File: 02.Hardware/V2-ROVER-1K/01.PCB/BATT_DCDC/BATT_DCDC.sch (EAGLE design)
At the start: 44 parts, among them K1 FLEX8, K2 FLEX6, Q1 NVTFS9D6P04M8LTAG, Q2 2N7002PW, Q5 2N7002PW, U1 MCP6071T-E/OT, U3 TPS55330RTET, U7 MCP6071T-E/OT

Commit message: Revision Silk y BOM
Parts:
- R10: value 330 -> 330R
- R3, R7: value 2.4k -> 2k4
- R38, R39: value 78.7k -> 78k7
- R43: value 78.7k -> 30k
- R5: value 33 -> 33R
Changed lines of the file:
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@@
 <part name="L1" library="Inductance_2.2uH" deviceset="74437349100" device="" value="2.2uH - 74437346022"/>
 <part name="D2" library="B520C-13-F" deviceset="B520C-13-F" device=""/>
-<part name="R38" library="SparkFun-Resistors" deviceset="RESISTOR" device="0402" value="78.7k"/>
+<part name="R38" library="SparkFun-Resistors" deviceset="RESISTOR" device="0402" value="78k7"/>
 <part name="GND17" library="SparkFun" deviceset="GND" device=""/>
 <part name="GND24" library="SparkFun" deviceset="GND" device=""/>
@@
 <part name="C19" library="Wurth_Elektronik_Passive_Capacitors_rev19a" library_urn="urn:adsk.eagle:library:491551" deviceset="WCAP-CSGP_1210" device="" package3d_urn="urn:adsk.eagle:package:491820/3" technology="_885012109003" value="47uF 25V"/>
 <part name="GND28" library="SparkFun" deviceset="GND" device=""/>
-<part name="R39" library="SparkFun-Resistors" library_urn="urn:adsk.eagle:library:532" deviceset="RESISTOR" device="0402" package3d_urn="urn:adsk.eagle:package:39657/1" value="78.7k"/>
+<part name="R39" library="SparkFun-Resistors" library_urn="urn:adsk.eagle:library:532" deviceset="RESISTOR" device="0402" package3d_urn="urn:adsk.eagle:package:39657/1" value="78k7"/>
 <part name="C21" library="SparkFun-Capacitors" deviceset="2.2NF/2200PF" device="-0603-50V-10%" value="2.2nF"/>
 <part name="R41" library="SparkFun-Resistors" library_urn="urn:adsk.eagle:library:532" deviceset="RESISTOR" device="0402" package3d_urn="urn:adsk.eagle:package:39657/1" value="56k2"/>
 <part name="C22" library="SparkFun-Capacitors" deviceset="270PF" device="-0603-50V-5%" value="270PF"/>
 <part name="GND30" library="SparkFun" deviceset="GND" device=""/>
-<part name="R43" library="SparkFun-Resistors" deviceset="RESISTOR" device="0402" value="78.7k"/>
+<part name="R43" library="SparkFun-Resistors" deviceset="RESISTOR" device="0402" value="30k"/>
 <part name="C12" library="Wurth_Elektronik_Passive_Capacitors_rev19a" library_urn="urn:adsk.eagle:library:491551" deviceset="WCAP-CSGP_1210" device="" package3d_urn="urn:adsk.eagle:package:491820/3" technology="_885012109003" value="47uF 16V"/>
 <part name="Q2" library="SparkFun-DiscreteSemi" deviceset="MOSFET-NCHANNEL" device="2N7002PW" value="2N7002PW"/>
@@
 <part name="GND9" library="SparkFun" deviceset="GND" device=""/>
 <part name="R4" library="SparkFun-Resistors" library_urn="urn:adsk.eagle:library:532" deviceset="RESISTOR" device="0402" package3d_urn="urn:adsk.eagle:package:39657/1" value="100k"/>
-<part name="R5" library="SparkFun-Resistors" library_urn="urn:adsk.eagle:library:532" deviceset="RESISTOR" device="0402" package3d_urn="urn:adsk.eagle:package:39657/1" value="33"/>
+<part name="R5" library="SparkFun-Resistors" library_urn="urn:adsk.eagle:library:532" deviceset="RESISTOR" device="0402" package3d_urn="urn:adsk.eagle:package:39657/1" value="33R"/>
 <part name="C24" library="SparkFun-Capacitors" deviceset="0.1UF" device="-0603-25V-(+80/-20%)" value="0.1uF"/>
 <part name="GND50" library="SparkFun" deviceset="GND" device=""/>
@@
 <part name="SUPPLY4" library="SparkFun-PowerSymbols" library_urn="urn:adsk.eagle:library:530" deviceset="VCC" device=""/>
 <part name="U7" library="MCP6071" deviceset="MCP6071T-E/OT" device=""/>
-<part name="R3" library="SparkFun-Resistors" deviceset="RESISTOR" device="0603" value="2.4k"/>
+<part name="R3" library="SparkFun-Resistors" deviceset="RESISTOR" device="0603" value="2k4"/>
 <part name="GND11" library="SparkFun" deviceset="GND" device=""/>
 <part name="R6" library="SparkFun-Resistors" deviceset="RESISTOR" device="0603" value="62k"/>
-<part name="R7" library="SparkFun-Resistors" deviceset="RESISTOR" device="0603" value="2.4k"/>
+<part name="R7" library="SparkFun-Resistors" deviceset="RESISTOR" device="0603" value="2k4"/>
 <part name="C1" library="microbuilder" deviceset="CAP_CERAMIC" device="0603_NO" value="1u"/>
 <part name="C4" library="microbuilder" deviceset="CAP_CERAMIC" device="0603_NO" value="1u"/>
@@
 <part name="K1" library="Flex_3mm" deviceset="FLEX8" device=""/>
 <part name="R9" library="SparkFun-Resistors" deviceset="RESISTOR" device="0402" value="7k5"/>
-<part name="R10" library="SparkFun-Resistors" library_urn="urn:adsk.eagle:library:532" deviceset="RESISTOR" device="0402" package3d_urn="urn:adsk.eagle:package:39657/1" value="330"/>
+<part name="R10" library="SparkFun-Resistors" library_urn="urn:adsk.eagle:library:532" deviceset="RESISTOR" device="0402" package3d_urn="urn:adsk.eagle:package:39657/1" value="330R"/>
 </parts>
 <sheets>

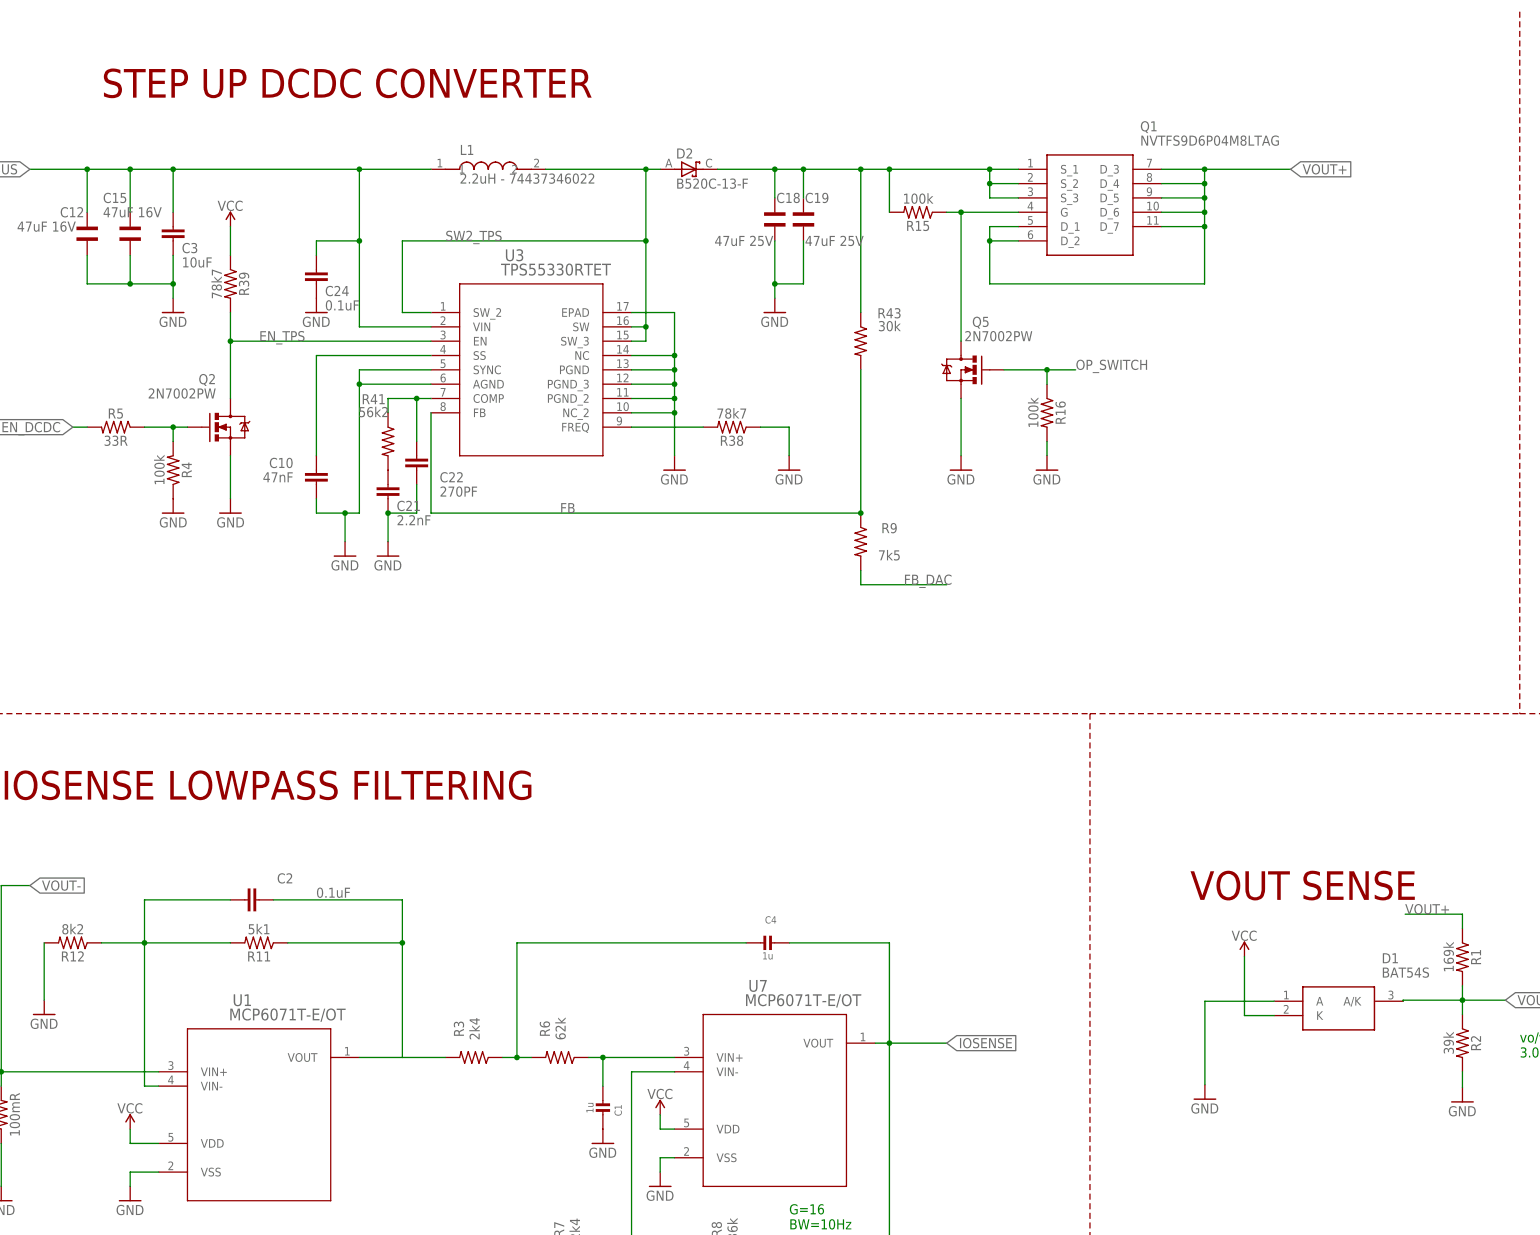
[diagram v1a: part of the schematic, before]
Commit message: Revision 2 - Release candidate (v1)
Se añade resistencia de FB que faltaba (R13)
Se corrige el valor de R9
Se separa la masa de señal (no potencia) de U3 a AGND
Se añaden condensadores de desacoplo para U1 y U7
Corregido el encapsulado de D1 a SOT323
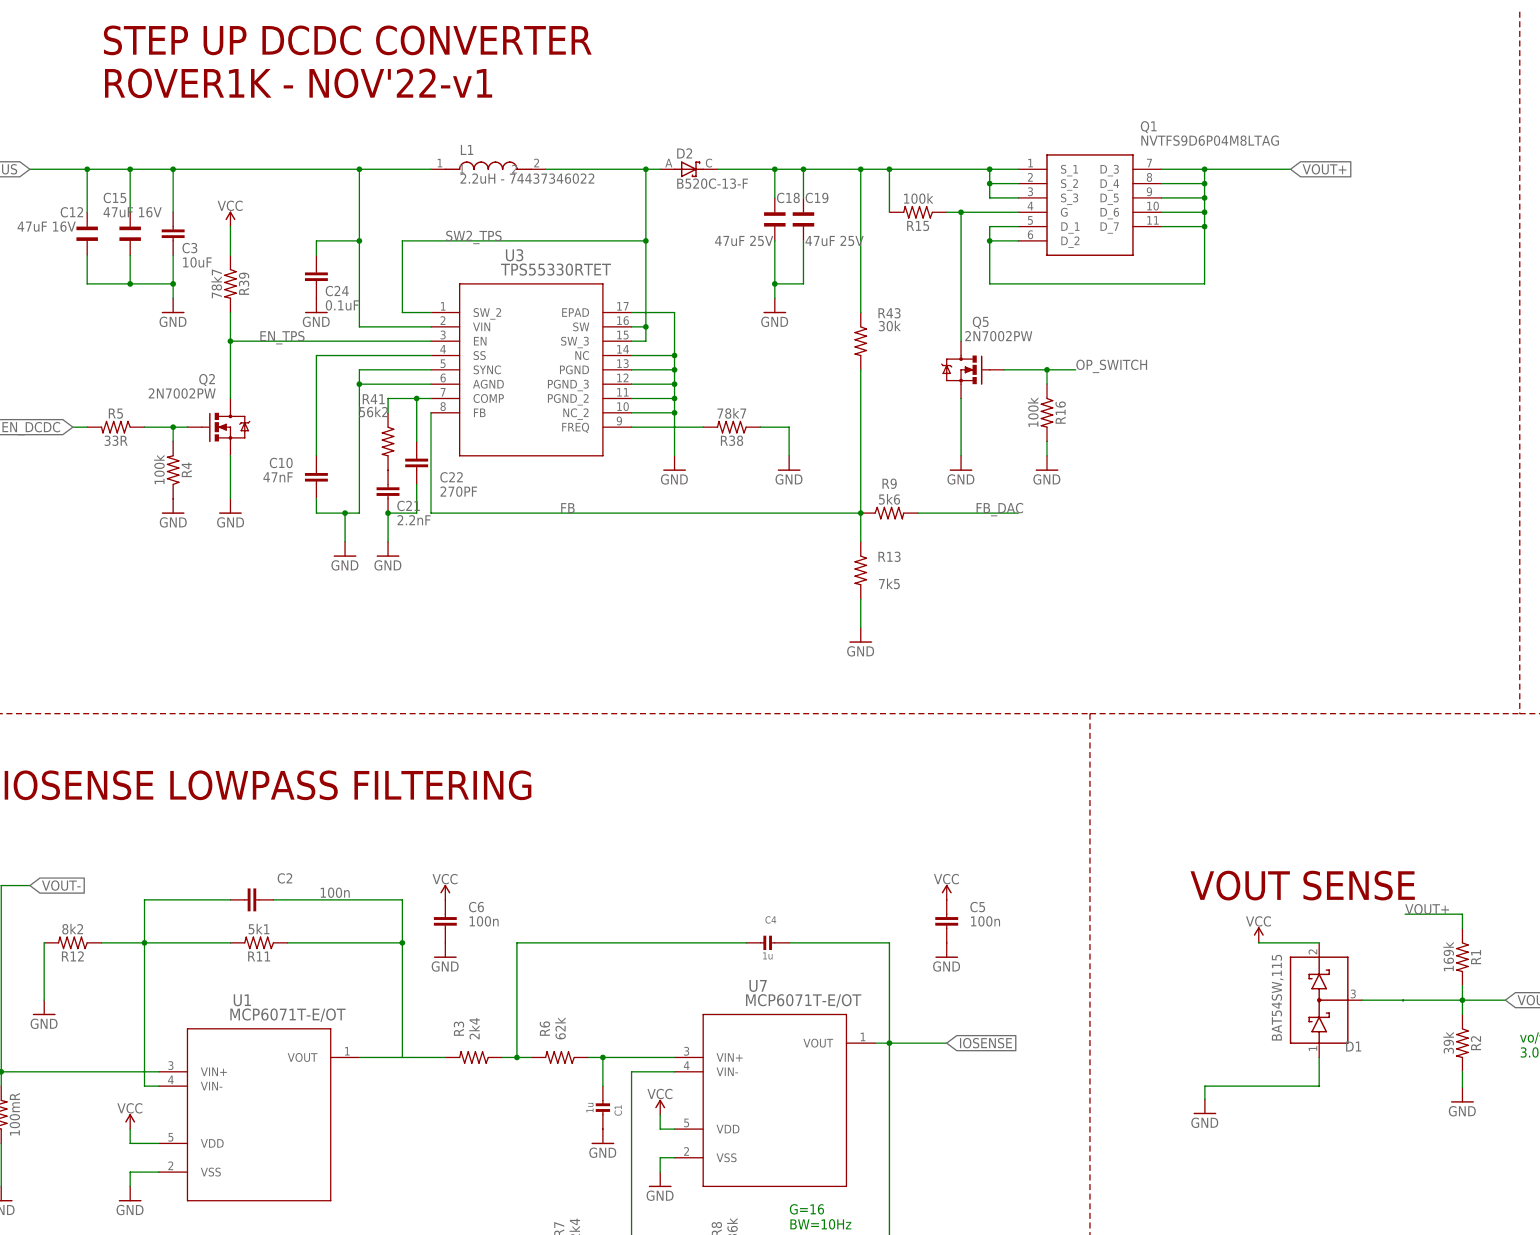
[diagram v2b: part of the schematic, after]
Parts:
- added C5, C6: 100n, SparkFun-Capacitors:0.1UF-0603-25V-(+80/-20%)
- added R13: 7k5, SparkFun-Resistors:RESISTOR0402
- C2: value 0.1uF -> 100n
- D1: value BAT54S -> BAT54SW,115; device BAT54S:BAT54S -> BAT54SW_115:BAT54SW,115
- R9: value 7k5 -> 5k6
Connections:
- net FB: now also R13.1
- net GND: now also C5.2, C6.2, R13.2
- net VCC: now also C5.1, C6.1, D1.C; no longer D1.K
- net VOUTSENSE: now also D1.A-C; no longer D1.A/K
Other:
- note added: "STEP UP DCDC CONVERTER ROVER1K - NOV'22-v1"
- note removed: "STEP UP DCDC CONVERTER"
- moved on the sheet: R9

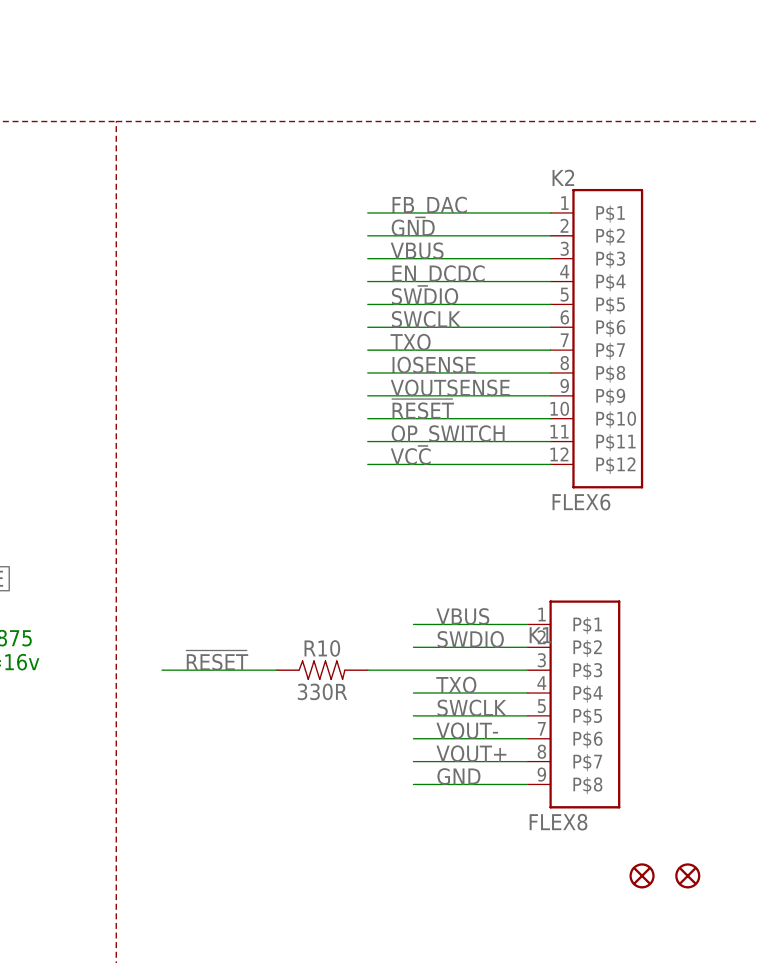
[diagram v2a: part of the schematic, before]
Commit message: Cambio de faja por conector interPCB. Issue #1
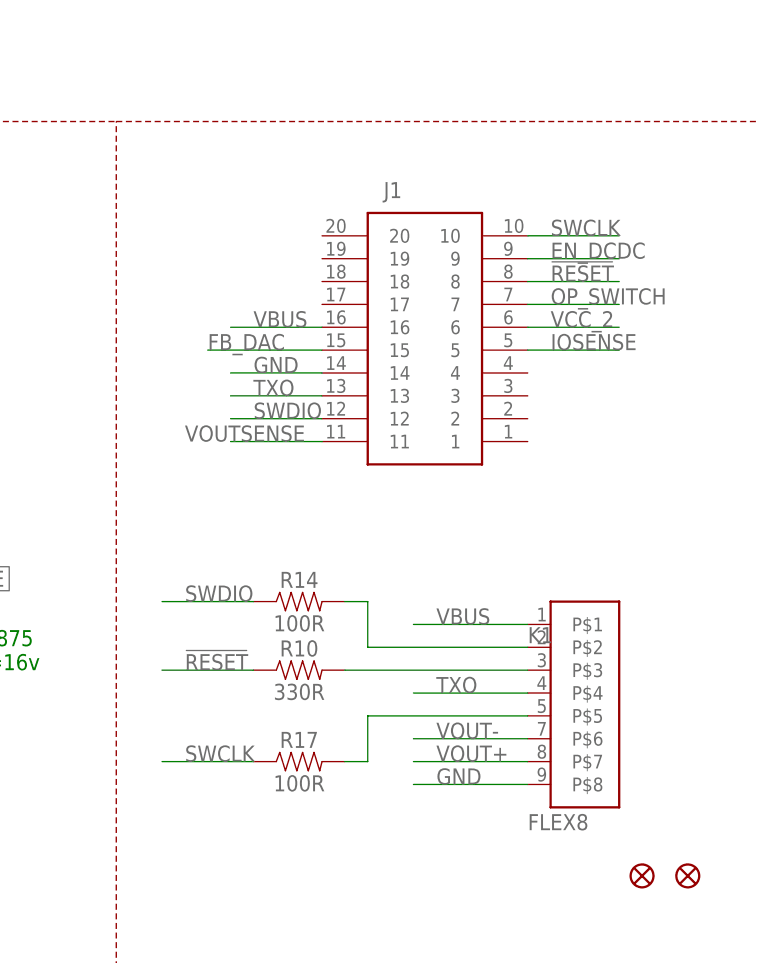
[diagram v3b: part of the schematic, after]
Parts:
- removed K2: FLEX6, Flex:FLEX6
- added J1: DF40C-20DP-0.4V_51_, DF40C-20DP-0.4V_51_:DF40C-20DP-0.4V_51_
- added R14, R17: 100R, SparkFun-Resistors:RESISTOR0402
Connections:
- new net N$10: K1.P$5, R17.2
- new net N$9: K1.P$2, R14.2
- new net VCC_2: J1.6
- net !RESET: now also J1.8; no longer K2.P$10
- net EN_DCDC: now also J1.9; no longer K2.P$4
- net FB_DAC: now also J1.15; no longer K2.P$1
- net GND: now also J1.14; no longer K2.P$2
- net IOSENSE: now also J1.5; no longer K2.P$8
- net OP_SWITCH: now also J1.7; no longer K2.P$11
- net SWCLK: now also J1.10, R17.1; no longer K1.P$5, K2.P$6
- net SWDIO: now also J1.12, R14.1; no longer K1.P$2, K2.P$5
- net TXO: now also J1.13; no longer K2.P$7
- net VBUS: now also J1.16; no longer K2.P$3
- net VCC: no longer K2.P$12
- net VOUTSENSE: now also J1.11; no longer K2.P$9
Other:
- moved on the sheet: R10
